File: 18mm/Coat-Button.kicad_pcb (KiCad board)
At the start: 2 copper layers, 18 x 18 mm, 43 parts, among them IC1 MADW__ATTINY13-MM, P1 CONN_1, P2 CONN_1, P3 CONN_1, P4 CONN_1, Q1 DMG1012T, Q2 DMG1012T

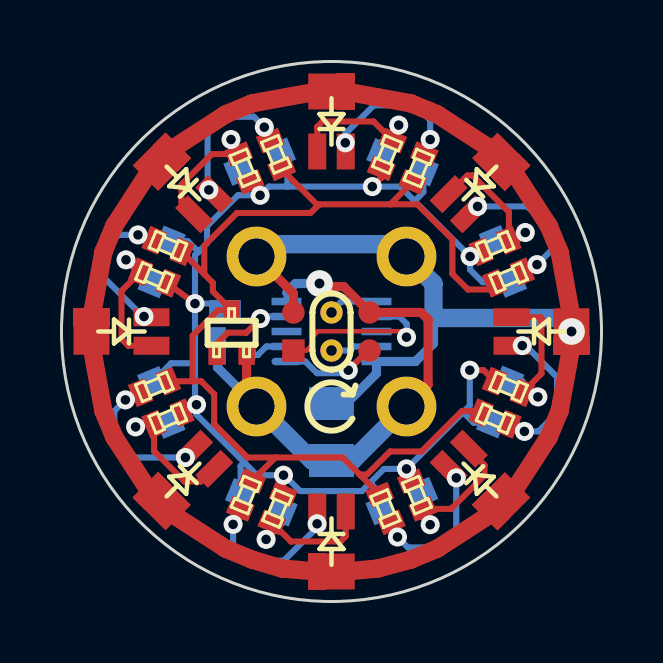
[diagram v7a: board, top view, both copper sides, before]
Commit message: Added a bit of silkscreen art.
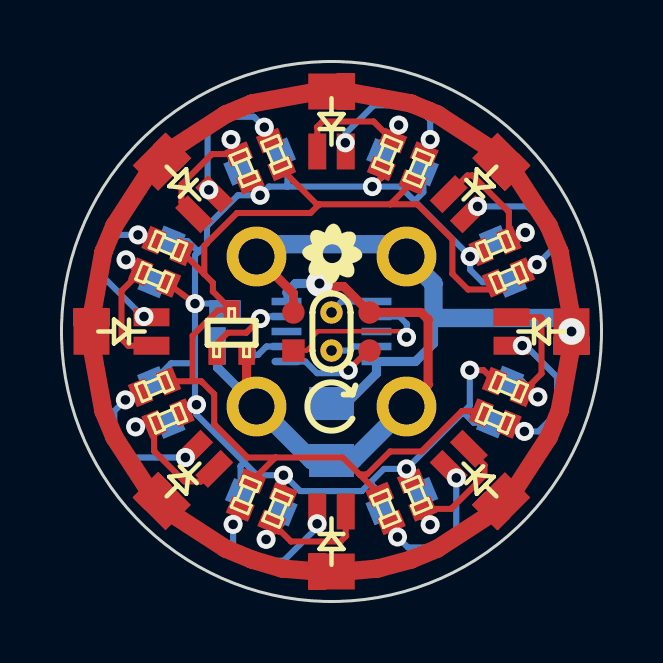
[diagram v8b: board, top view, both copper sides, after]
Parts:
- added G3: floral-shape_silkscreen_2mm, floral-shape_silkscreen_2mm, F.Cu at (75.0, 59.4)
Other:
- board text added: "0.22.b"
- board text removed: "0.22.a"
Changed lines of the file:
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@@
-(kicad_pcb (version 3) (host pcbnew "(2013-10-02 BZR 4359)-product")
+(kicad_pcb (version 3) (host pcbnew "(2013-10-07 BZR 4376)-product")
   (general
     (links 80)
@@
     (tracks 412)
     (zones 0)
-    (modules 43)
+    (modules 44)
     (nets 27)
   )
@@
   (title_block
     (title Coat-Button)
-    (date "03 Oct 2013")
-    (rev 0.22.a)
+    (date "08 Oct 2013")
+    (rev 0.22.b)
     (company "2013 - blog.spitzenpfeil.org")
   )
@@
       (net 20 Net-<LED8-Pad2>))
   )
-  (gr_text 0.22.a (at 75 54.19) (layer B.SilkS)
+  (module floral-shape_silkscreen_2mm (layer F.Cu)
+    (at 75.03 59.4 45)
+    (fp_text reference G3 (at 0 1.18872 45) (layer F.SilkS) hide
+      (effects (font (size 0.127 0.127) (thickness 0.00508)))
+    )
+    (fp_text value floral-shape_silkscreen_2mm (at 0 -1.18872 45) (layer F.SilkS) hide
+      (effects (font (size 0.03302 0.03302) (thickness 0.00508)))
+    )
+    (fp_poly (pts (xy 0.9906 0.03556) (xy 0.9906 0.06096) (xy 0.98552 0.08636) (xy 0.9779 0.11176)
+      (xy 0.9652 0.13462) (xy 0.94996 0.15748) (xy 0.9398 0.17272) (xy 0.91948 0.19304)
+      (xy 0.89408 0.21336) (xy 0.86868 0.23114) (xy 0.8382 0.24892) (xy 0.80518 0.2667)
+      (xy 0.76962 0.28194) (xy 0.73152 0.29718) (xy 0.69088 0.30734) (xy 0.68326 0.30988)
+      (xy 0.67564 0.31242) (xy 0.66802 0.31496) (xy 0.66294 0.3175) (xy 0.66294 0.3175)
+      (xy 0.66294 0.3175) (xy 0.66548 0.32512) (xy 0.67056 0.33528) (xy 0.67564 0.34544)
+      (xy 0.68072 0.35814) (xy 0.68834 0.37084) (xy 0.69342 0.38354) (xy 0.6985 0.3937)
+      (xy 0.70104 0.40386) (xy 0.70104 0.40386) (xy 0.71374 0.43942) (xy 0.72136 0.47498)
+      (xy 0.72644 0.508) (xy 0.72898 0.54356) (xy 0.72898 0.57404) (xy 0.72644 0.60452)
+      (xy 0.72136 0.635) (xy 0.71374 0.66294) (xy 0.70358 0.68834) (xy 0.68834 0.7112)
+      (xy 0.68326 0.71882) (xy 0.66548 0.73914) (xy 0.64516 0.75438) (xy 0.62484 0.76962)
+      (xy 0.60198 0.77978) (xy 0.57404 0.7874) (xy 0.54864 0.78994) (xy 0.51816 0.79248)
+      (xy 0.48768 0.78994) (xy 0.45466 0.78486) (xy 0.42926 0.77978) (xy 0.40132 0.77216)
+      (xy 0.3683 0.75946) (xy 0.33528 0.74676) (xy 0.30734 0.73406) (xy 0.30734 -0.00254)
+      (xy 0.30734 -0.02032) (xy 0.3048 -0.03556) (xy 0.3048 -0.04572) (xy 0.29718 -0.07874)
+      (xy 0.28702 -0.11176) (xy 0.27178 -0.14224) (xy 0.25654 -0.17018) (xy 0.23622 -0.19812)
+      (xy 0.2159 -0.22098) (xy 0.1905 -0.24384) (xy 0.16256 -0.26416) (xy 0.13462 -0.2794)
+      (xy 0.10414 -0.29464) (xy 0.07874 -0.30226) (xy 0.04572 -0.30988) (xy 0.0127 -0.31496)
+      (xy -0.01778 -0.31496) (xy -0.04826 -0.31242) (xy -0.08128 -0.3048) (xy -0.11176 -0.29718)
+      (xy -0.14224 -0.28448) (xy -0.17018 -0.26924) (xy -0.19558 -0.25146) (xy -0.22098 -0.23114)
+      (xy -0.24384 -0.20828) (xy -0.26416 -0.18288) (xy -0.28194 -0.15494) (xy -0.29718 -0.12446)
+      (xy -0.30226 -0.11176) (xy -0.30988 -0.08382) (xy -0.3175 -0.05588) (xy -0.32004 -0.0254)
+      (xy -0.32258 0) (xy -0.32004 0.02794) (xy -0.3175 0.05842) (xy -0.30988 0.08382)
+      (xy -0.30226 0.11176) (xy -0.28956 0.1397) (xy -0.28702 0.14224) (xy -0.27178 0.17272)
+      (xy -0.25146 0.19812) (xy -0.2286 0.22352) (xy -0.2032 0.24638) (xy -0.1778 0.26416)
+      (xy -0.14732 0.28194) (xy -0.11684 0.29464) (xy -0.08636 0.3048) (xy -0.05334 0.31242)
+      (xy -0.03048 0.31496) (xy -0.02286 0.31496) (xy -0.01778 0.31496) (xy -0.01524 0.31496)
+      (xy -0.0127 0.31496) (xy -0.0127 0.31496) (xy -0.00762 0.31496) (xy 0 0.31496)
+      (xy 0.00762 0.31496) (xy 0.01016 0.31496) (xy 0.04572 0.30988) (xy 0.0762 0.30226)
+      (xy 0.10668 0.2921) (xy 0.13208 0.28194) (xy 0.16256 0.26416) (xy 0.1905 0.24384)
+      (xy 0.2159 0.22098) (xy 0.23622 0.19812) (xy 0.25654 0.17018) (xy 0.27432 0.1397)
+      (xy 0.28702 0.10922) (xy 0.29718 0.0762) (xy 0.3048 0.04572) (xy 0.3048 0.03048)
+      (xy 0.30734 0.01524) (xy 0.30734 -0.00254) (xy 0.30734 0.73406) (xy 0.30226 0.73152)
+      (xy 0.26924 0.71374) (xy 0.26416 0.7112) (xy 0.25654 0.70612) (xy 0.24892 0.70358)
+      (xy 0.24384 0.70104) (xy 0.2413 0.6985) (xy 0.2413 0.6985) (xy 0.2413 0.70104)
+      (xy 0.23876 0.70612) (xy 0.23622 0.7112) (xy 0.23368 0.71882) (xy 0.21844 0.75946)
+      (xy 0.20066 0.79756) (xy 0.18288 0.83312) (xy 0.16002 0.86868) (xy 0.13716 0.89916)
+      (xy 0.11684 0.91948) (xy 0.09144 0.94234) (xy 0.06604 0.96012) (xy 0.04064 0.97536)
+      (xy 0.01524 0.98552) (xy -0.00508 0.99314) (xy -0.01778 0.99568) (xy -0.03302 0.99822)
+      (xy -0.04826 0.99822) (xy -0.0635 0.99822) (xy -0.0762 0.99822) (xy -0.08128 0.99568)
+      (xy -0.10668 0.9906) (xy -0.13208 0.98044) (xy -0.15494 0.9652) (xy -0.1778 0.94742)
+      (xy -0.20066 0.9271) (xy -0.22098 0.90424) (xy -0.23876 0.8763) (xy -0.25654 0.84582)
+      (xy -0.27432 0.8128) (xy -0.28448 0.79248) (xy -0.28956 0.77724) (xy -0.29718 0.75946)
+      (xy -0.30226 0.73914) (xy -0.30988 0.72136) (xy -0.31496 0.70358) (xy -0.32004 0.68834)
+      (xy -0.32512 0.66802) (xy -0.35052 0.68072) (xy -0.39116 0.70104) (xy -0.4318 0.71628)
+      (xy -0.47244 0.72644) (xy -0.51308 0.73406) (xy -0.52832 0.7366) (xy -0.54102 0.7366)
+      (xy -0.55626 0.73914) (xy -0.57404 0.7366) (xy -0.58928 0.7366) (xy -0.60452 0.7366)
+      (xy -0.61976 0.73406) (xy -0.62484 0.73406) (xy -0.65532 0.72644) (xy -0.68326 0.71628)
+      (xy -0.70612 0.70358) (xy -0.72898 0.68834) (xy -0.74676 0.67056) (xy -0.76454 0.65278)
+      (xy -0.77724 0.62992) (xy -0.7874 0.60452) (xy -0.79502 0.57912) (xy -0.79756 0.56388)
+      (xy -0.8001 0.54356) (xy -0.8001 0.52324) (xy -0.79756 0.49784) (xy -0.79502 0.47244)
+      (xy -0.78994 0.44704) (xy -0.7874 0.43434) (xy -0.77978 0.40894) (xy -0.76962 0.38354)
+      (xy -0.75946 0.3556) (xy -0.74676 0.32766) (xy -0.73406 0.30226) (xy -0.72136 0.27432)
+      (xy -0.71882 0.26924) (xy -0.71374 0.26162) (xy -0.70866 0.25654) (xy -0.70612 0.25146)
+      (xy -0.70612 0.24892) (xy -0.70612 0.24892) (xy -0.70866 0.24638) (xy -0.71374 0.24638)
+      (xy -0.71882 0.24384) (xy -0.7239 0.2413) (xy -0.74422 0.23622) (xy -0.76454 0.2286)
+      (xy -0.7874 0.21844) (xy -0.80772 0.20828) (xy -0.84074 0.1905) (xy -0.87122 0.17018)
+      (xy -0.89662 0.14986) (xy -0.92202 0.12954) (xy -0.94488 0.10668) (xy -0.96266 0.08128)
+      (xy -0.9779 0.05842) (xy -0.9906 0.03302) (xy -0.99822 0.00762) (xy -1.00584 -0.01778)
+      (xy -1.00584 -0.04318) (xy -1.00584 -0.05334) (xy -1.0033 -0.07874) (xy -0.99568 -0.10414)
+      (xy -0.98552 -0.127) (xy -0.97028 -0.14986) (xy -0.9525 -0.17272) (xy -0.93218 -0.19304)
+      (xy -0.90932 -0.21336) (xy -0.88138 -0.23368) (xy -0.8509 -0.25146) (xy -0.81788 -0.26924)
+      (xy -0.77978 -0.28448) (xy -0.74168 -0.29718) (xy -0.70612 -0.30734) (xy -0.67818 -0.3175)
+      (xy -0.69088 -0.3429) (xy -0.70866 -0.38354) (xy -0.7239 -0.42164) (xy -0.73406 -0.45974)
+      (xy -0.74168 -0.4953) (xy -0.74422 -0.5334) (xy -0.74422 -0.5715) (xy -0.74422 -0.57404)
+      (xy -0.74168 -0.60452) (xy -0.7366 -0.635) (xy -0.72898 -0.66294) (xy -0.71882 -0.68834)
+      (xy -0.70358 -0.7112) (xy -0.68834 -0.73152) (xy -0.6858 -0.73406) (xy -0.66548 -0.75184)
+      (xy -0.64516 -0.76708) (xy -0.61976 -0.77724) (xy -0.59436 -0.78486) (xy -0.56642 -0.78994)
+      (xy -0.53848 -0.79248) (xy -0.508 -0.78994) (xy -0.47498 -0.7874) (xy -0.46482 -0.78486)
+      (xy -0.43688 -0.77724) (xy -0.4064 -0.76962) (xy -0.37592 -0.75692) (xy -0.3429 -0.74422)
+      (xy -0.30988 -0.72644) (xy -0.28194 -0.7112) (xy -0.27432 -0.70866) (xy -0.2667 -0.70358)
+      (xy -0.25908 -0.70104) (xy -0.25654 -0.6985) (xy -0.25654 -0.6985) (xy -0.254 -0.70104)
+      (xy -0.254 -0.70612) (xy -0.25146 -0.7112) (xy -0.24892 -0.71628) (xy -0.23876 -0.75184)
+      (xy -0.22352 -0.78486) (xy -0.20574 -0.81788) (xy -0.18796 -0.84836) (xy -0.16764 -0.8763)
+      (xy -0.14732 -0.90424) (xy -0.12446 -0.9271) (xy -0.1143 -0.93472) (xy -0.09144 -0.95504)
+      (xy -0.06604 -0.97028) (xy -0.04064 -0.98298) (xy -0.01524 -0.9906) (xy 0.00762 -0.99568)
+      (xy 0.03302 -0.99822) (xy 0.05842 -0.99822) (xy 0.08382 -0.9906) (xy 0.10922 -0.98298)
+      (xy 0.13208 -0.97028) (xy 0.1397 -0.9652) (xy 0.16256 -0.94996) (xy 0.18288 -0.9271)
+      (xy 0.20574 -0.90424) (xy 0.22352 -0.8763) (xy 0.2413 -0.84582) (xy 0.25908 -0.81026)
+      (xy 0.27432 -0.7747) (xy 0.28956 -0.73406) (xy 0.29972 -0.70358) (xy 0.30988 -0.66802)
+      (xy 0.33528 -0.68072) (xy 0.37084 -0.6985) (xy 0.40386 -0.7112) (xy 0.43942 -0.72136)
+      (xy 0.47244 -0.72898) (xy 0.50546 -0.7366) (xy 0.53848 -0.73914) (xy 0.56896 -0.73914)
+      (xy 0.59944 -0.73406) (xy 0.62738 -0.72898) (xy 0.65278 -0.72136) (xy 0.67818 -0.7112)
+      (xy 0.70104 -0.6985) (xy 0.72136 -0.68326) (xy 0.73914 -0.66548) (xy 0.75184 -0.64516)
+      (xy 0.76454 -0.6223) (xy 0.7747 -0.59944) (xy 0.78232 -0.5715) (xy 0.78486 -0.54356)
+      (xy 0.78486 -0.51308) (xy 0.78232 -0.4826) (xy 0.7747 -0.44958) (xy 0.76708 -0.41402)
+      (xy 0.75438 -0.37846) (xy 0.73914 -0.3429) (xy 0.72136 -0.3048) (xy 0.70612 -0.27686)
+      (xy 0.70104 -0.2667) (xy 0.69596 -0.25908) (xy 0.69342 -0.254) (xy 0.69088 -0.24892)
+      (xy 0.69088 -0.24892) (xy 0.69342 -0.24638) (xy 0.6985 -0.24638) (xy 0.70358 -0.24384)
+      (xy 0.72136 -0.23876) (xy 0.73914 -0.23114) (xy 0.75946 -0.22352) (xy 0.78232 -0.21336)
+      (xy 0.80264 -0.2032) (xy 0.82042 -0.19304) (xy 0.83058 -0.18796) (xy 0.86106 -0.16764)
+      (xy 0.889 -0.14478) (xy 0.91186 -0.12192) (xy 0.93472 -0.09906) (xy 0.9525 -0.07366)
+      (xy 0.9525 -0.07366) (xy 0.96266 -0.05588) (xy 0.97028 -0.04318) (xy 0.9779 -0.0254)
+      (xy 0.98044 -0.01524) (xy 0.98806 0.01016) (xy 0.9906 0.03556) (xy 0.9906 0.03556)) (layer F.SilkS) (width 0.00254))
+  )
+  (gr_text 0.22.b (at 75 54.19) (layer B.SilkS)
     (effects (font (size 1 1) (thickness 0.2)) (justify mirror))
   )
